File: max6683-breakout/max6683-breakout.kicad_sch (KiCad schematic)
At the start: 11 parts, among them J1 Conn_01x05, J2 Conn_01x05, U1 MAX6683

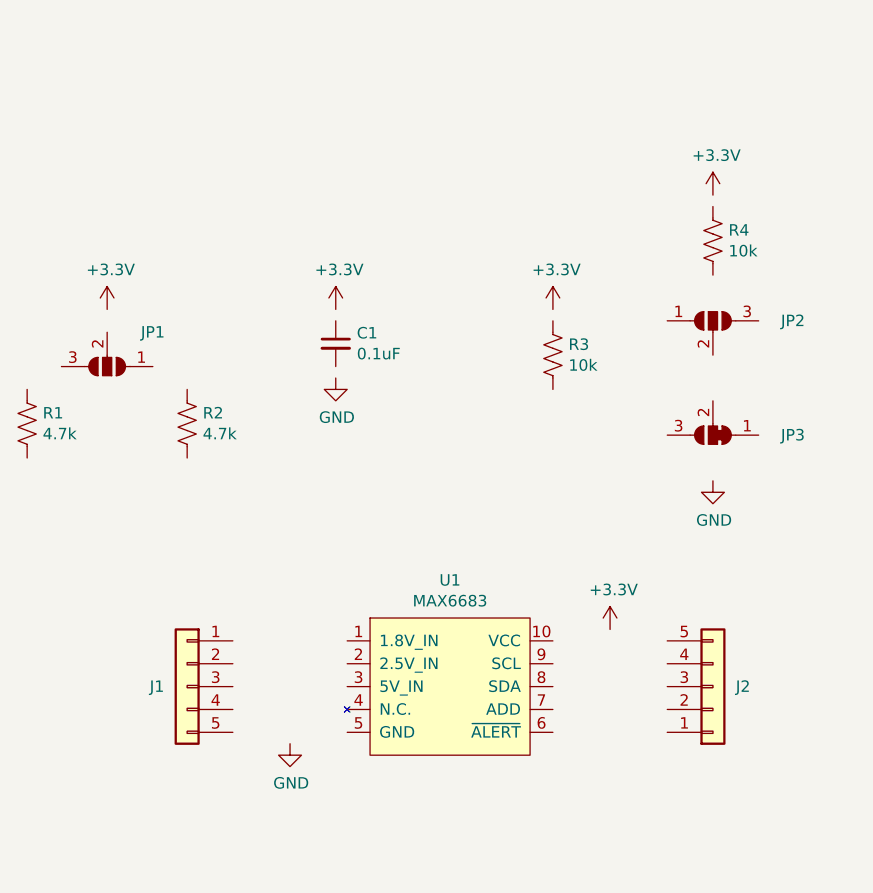
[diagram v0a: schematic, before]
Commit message: Connect schematic nets
Supports #44.
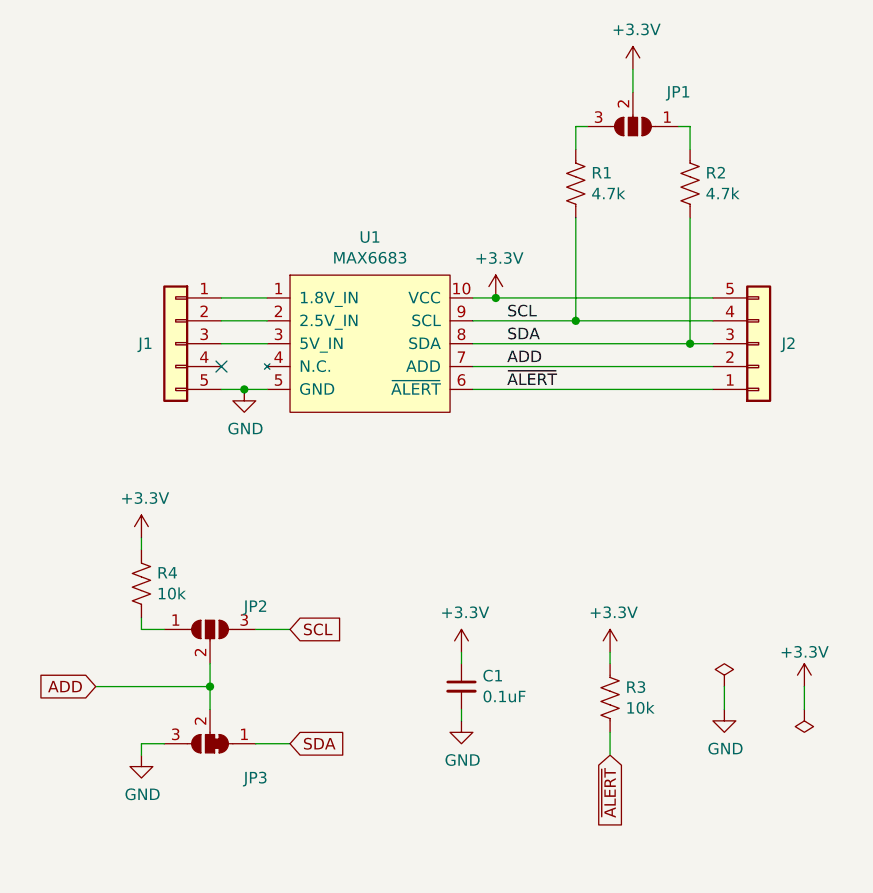
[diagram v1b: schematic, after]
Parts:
- JP1, JP2: value (none) -> SolderJumper_3_Open; footprint (none) -> Jumper:SolderJumper-3_P1.3mm_Open_RoundedPad1.0x1.5mm
- JP3: value (none) -> SolderJumper_3_Bridged12; footprint (none) -> Jumper:SolderJumper-3_P1.3mm_Bridged12_RoundedPad1.0x1.5mm
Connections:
- net +3V3: now also C1.1, J2.5 (Pin_5), JP1.2 (C), R3.1, R4.1, U1.10 (VCC)
- net GND: now also C1.2, J1.5 (Pin_5), JP3.3 (B), U1.5 (GND)
- net at U1.1 (1.8V_IN): now also J1.1 (Pin_1)
- net at U1.2 (2.5V_IN): now also J1.2 (Pin_2)
- net at U1.3 (5V_IN): now also J1.3 (Pin_3)
- net ~{ALERT}: now reaches U1.6 (~{ALERT})
- net ~{ALERT}: now also J2.1 (Pin_1), R3.2
- net ADD: now reaches U1.7 (ADD)
- net ADD: now also J2.2 (Pin_2), JP2.2 (C), JP3.2 (C)
- net SDA: now reaches U1.8 (SDA)
- net SDA: now also J2.3 (Pin_3), JP3.1 (A), R2.2
- net SCL: now reaches U1.9 (SCL)
- net SCL: now also J2.4 (Pin_4), JP2.3 (B), R1.2
- net at R1.1: now also JP1.3 (B)
- net at R2.1: now also JP1.1 (A)
- net at R4.2: now also JP2.1 (A)
- no-connect marks 0 -> 1
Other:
- moved on the sheet: C1, J1, J2, JP1, JP2, JP3, R1, R2, R3, R4, U1

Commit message: Update I2C pullup resistor value
Supports #44.
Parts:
- R1, R2: value 4.7k -> (none); footprint Resistor_SMD:R_0603_1608Metric -> (none); Part Number ERJ-3EKF4701V -> ERJ-3EKF2201V
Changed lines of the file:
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@@
       (effects (font (size 1.27 1.27)) (justify left))
     )
-    (property "Value" "4.7k" (id 1) (at 160.4772 64.643 0)
-      (effects (font (size 1.27 1.27)) (justify left))
-    )
-    (property "Footprint" "Resistor_SMD:R_0603_1608Metric" (id 2) (at 159.766 63.754 90)
+    (property "Value" "" (id 1) (at 160.4772 64.643 0)
+      (effects (font (size 1.27 1.27)) (justify left))
+    )
+    (property "Footprint" "" (id 2) (at 159.766 63.754 90)
       (effects (font (size 1.27 1.27)) hide)
     )
@@
       (effects (font (size 1.27 1.27)) hide)
     )
-    (property "Part Number" "ERJ-3EKF4701V" (id 4) (at 158.75 63.5 0)
+    (property "Part Number" "ERJ-3EKF2201V" (id 4) (at 158.75 63.5 0)
       (effects (font (size 1.27 1.27)) hide)
     )
@@
       (effects (font (size 1.27 1.27)) (justify left))
     )
-    (property "Value" "4.7k" (id 1) (at 173.1772 64.643 0)
-      (effects (font (size 1.27 1.27)) (justify left))
-    )
-    (property "Footprint" "Resistor_SMD:R_0603_1608Metric" (id 2) (at 172.466 63.754 90)
+    (property "Value" "" (id 1) (at 173.1772 64.643 0)
+      (effects (font (size 1.27 1.27)) (justify left))
+    )
+    (property "Footprint" "" (id 2) (at 172.466 63.754 90)
       (effects (font (size 1.27 1.27)) hide)
     )
@@
       (effects (font (size 1.27 1.27)) hide)
     )
-    (property "Part Number" "ERJ-3EKF4701V" (id 4) (at 171.45 63.5 0)
+    (property "Part Number" "ERJ-3EKF2201V" (id 4) (at 171.45 63.5 0)
       (effects (font (size 1.27 1.27)) hide)
     )
@@
       (effects (font (size 1.27 1.27)) hide)
     )
-    (property "Value" "" (id 1) (at 175.26 115.57 0))
+    (property "Value" "PWR_FLAG" (id 1) (at 175.26 115.57 0))
     (property "Footprint" "" (id 2) (at 175.26 119.38 0)
       (effects (font (size 1.27 1.27)) hide)
@@
       (effects (font (size 1.27 1.27)) hide)
     )
-    (property "Value" "" (id 1) (at 184.15 125.73 0))
+    (property "Value" "PWR_FLAG" (id 1) (at 184.15 125.73 0))
     (property "Footprint" "" (id 2) (at 184.15 121.92 0)
       (effects (font (size 1.27 1.27)) hide)
@@
     )
     (path "/00000000-0000-0000-0000-00006201c9d1"
-      (reference "R1") (unit 1) (value "4.7k") (footprint "Resistor_SMD:R_0603_1608Metric")
+      (reference "R1") (unit 1) (value "2.2k") (footprint "Resistor_SMD:R_0603_1608Metric")
     )
     (path "/00000000-0000-0000-0000-0000620b838e"
-      (reference "R2") (unit 1) (value "4.7k") (footprint "Resistor_SMD:R_0603_1608Metric")
+      (reference "R2") (unit 1) (value "2.2k") (footprint "Resistor_SMD:R_0603_1608Metric")
     )
     (path "/00000000-0000-0000-0000-0000620b8c4a"

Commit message: Remove solder jumpers and power flags from BOM
Supports #44.
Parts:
- JP1, JP2: value SolderJumper_3_Open -> (none); footprint Jumper:SolderJumper-3_P1.3mm_Open_RoundedPad1.0x1.5mm -> (none); now left out of the parts list
- JP3: value SolderJumper_3_Bridged12 -> (none); footprint Jumper:SolderJumper-3_P1.3mm_Bridged12_RoundedPad1.0x1.5mm -> (none); now left out of the parts list
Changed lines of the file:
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@@
   )
   (symbol (lib_id "power:+3.3V") (at 165.1 50.8 0) (unit 1)
-    (in_bom yes) (on_board yes)
+    (in_bom no) (on_board yes)
     (property "Reference" "#PWR0101" (id 0) (at 165.1 54.61 0)
       (effects (font (size 1.27 1.27)) hide)
     )
-    (property "Value" "+3.3V" (id 1) (at 165.481 46.4058 0))
+    (property "Value" "" (id 1) (at 165.481 46.4058 0))
     (property "Footprint" "" (id 2) (at 165.1 50.8 0)
       (effects (font (size 1.27 1.27)) hide)
@@
   )
   (symbol (lib_id "power:+3.3V") (at 149.86 76.2 0) (unit 1)
-    (in_bom yes) (on_board yes)
+    (in_bom no) (on_board yes)
     (property "Reference" "#PWR0102" (id 0) (at 149.86 80.01 0)
       (effects (font (size 1.27 1.27)) hide)
     )
-    (property "Value" "+3.3V" (id 1) (at 150.241 71.8058 0))
+    (property "Value" "" (id 1) (at 150.241 71.8058 0))
     (property "Footprint" "" (id 2) (at 149.86 76.2 0)
       (effects (font (size 1.27 1.27)) hide)
@@
   )
   (symbol (lib_id "power:GND") (at 121.92 86.36 0) (unit 1)
-    (in_bom yes) (on_board yes)
+    (in_bom no) (on_board yes)
     (property "Reference" "#PWR0103" (id 0) (at 121.92 92.71 0)
       (effects (font (size 1.27 1.27)) hide)
     )
-    (property "Value" "GND" (id 1) (at 122.047 90.7542 0))
+    (property "Value" "" (id 1) (at 122.047 90.7542 0))
     (property "Footprint" "" (id 2) (at 121.92 86.36 0)
       (effects (font (size 1.27 1.27)) hide)
@@
   )
   (symbol (lib_id "power:GND") (at 110.49 127 0) (unit 1)
-    (in_bom yes) (on_board yes)
+    (in_bom no) (on_board yes)
     (property "Reference" "#PWR0104" (id 0) (at 110.49 133.35 0)
       (effects (font (size 1.27 1.27)) hide)
     )
-    (property "Value" "GND" (id 1) (at 110.617 131.3942 0))
+    (property "Value" "" (id 1) (at 110.617 131.3942 0))
     (property "Footprint" "" (id 2) (at 110.49 127 0)
       (effects (font (size 1.27 1.27)) hide)
@@
   )
   (symbol (lib_id "power:+3.3V") (at 146.05 115.57 0) (unit 1)
-    (in_bom yes) (on_board yes)
+    (in_bom no) (on_board yes)
     (property "Reference" "#PWR0105" (id 0) (at 146.05 119.38 0)
       (effects (font (size 1.27 1.27)) hide)
     )
-    (property "Value" "+3.3V" (id 1) (at 146.431 111.1758 0))
+    (property "Value" "" (id 1) (at 146.431 111.1758 0))
     (property "Footprint" "" (id 2) (at 146.05 115.57 0)
       (effects (font (size 1.27 1.27)) hide)
@@
   )
   (symbol (lib_id "power:GND") (at 146.05 123.19 0) (unit 1)
-    (in_bom yes) (on_board yes)
+    (in_bom no) (on_board yes)
     (property "Reference" "#PWR0106" (id 0) (at 146.05 129.54 0)
       (effects (font (size 1.27 1.27)) hide)
     )
-    (property "Value" "GND" (id 1) (at 146.177 127.5842 0))
+    (property "Value" "" (id 1) (at 146.177 127.5842 0))
     (property "Footprint" "" (id 2) (at 146.05 123.19 0)
       (effects (font (size 1.27 1.27)) hide)
@@
   )
   (symbol (lib_id "power:+3.3V") (at 162.56 115.57 0) (unit 1)
-    (in_bom yes) (on_board yes)
+    (in_bom no) (on_board yes)
     (property "Reference" "#PWR0107" (id 0) (at 162.56 119.38 0)
       (effects (font (size 1.27 1.27)) hide)
     )
-    (property "Value" "+3.3V" (id 1) (at 162.941 111.1758 0))
+    (property "Value" "" (id 1) (at 162.941 111.1758 0))
     (property "Footprint" "" (id 2) (at 162.56 115.57 0)
       (effects (font (size 1.27 1.27)) hide)
@@
   )
   (symbol (lib_id "power:+3.3V") (at 110.49 102.87 0) (unit 1)
-    (in_bom yes) (on_board yes)
+    (in_bom no) (on_board yes)
     (property "Reference" "#PWR0108" (id 0) (at 110.49 106.68 0)
       (effects (font (size 1.27 1.27)) hide)
     )
-    (property "Value" "+3.3V" (id 1) (at 110.871 98.4758 0))
+    (property "Value" "" (id 1) (at 110.871 98.4758 0))
     (property "Footprint" "" (id 2) (at 110.49 102.87 0)
       (effects (font (size 1.27 1.27)) hide)
@@
   )
   (symbol (lib_id "Jumper:SolderJumper_3_Bridged12") (at 118.11 125.73 180) (unit 1)
-    (in_bom yes) (on_board yes)
+    (in_bom no) (on_board yes)
     (property "Reference" "JP3" (id 0) (at 123.19 129.54 0))
-    (property "Value" "SolderJumper_3_Bridged12" (id 1) (at 118.11 129.54 0)
-      (effects (font (size 1.27 1.27)) hide)
-    )
-    (property "Footprint" "Jumper:SolderJumper-3_P1.3mm_Bridged12_RoundedPad1.0x1.5mm" (id 2) (at 118.11 125.73 0)
+    (property "Value" "" (id 1) (at 118.11 129.54 0)
+      (effects (font (size 1.27 1.27)) hide)
+    )
+    (property "Footprint" "" (id 2) (at 118.11 125.73 0)
       (effects (font (size 1.27 1.27)) hide)
     )
@@
   )
   (symbol (lib_id "power:GND") (at 175.26 121.92 0) (unit 1)
-    (in_bom yes) (on_board yes)
+    (in_bom no) (on_board yes)
     (property "Reference" "#PWR01" (id 0) (at 175.26 128.27 0)
       (effects (font (size 1.27 1.27)) hide)
     )
-    (property "Value" "GND" (id 1) (at 175.387 126.3142 0))
+    (property "Value" "" (id 1) (at 175.387 126.3142 0))
     (property "Footprint" "" (id 2) (at 175.26 121.92 0)
       (effects (font (size 1.27 1.27)) hide)
@@
   )
   (symbol (lib_id "power:+3.3V") (at 184.15 119.38 0) (unit 1)
-    (in_bom yes) (on_board yes)
+    (in_bom no) (on_board yes)
     (property "Reference" "#PWR02" (id 0) (at 184.15 123.19 0)
       (effects (font (size 1.27 1.27)) hide)
     )
-    (property "Value" "+3.3V" (id 1) (at 184.15 115.57 0))
+    (property "Value" "" (id 1) (at 184.15 115.57 0))
     (property "Footprint" "" (id 2) (at 184.15 119.38 0)
       (effects (font (size 1.27 1.27)) hide)
@@
   )
   (symbol (lib_id "power:PWR_FLAG") (at 175.26 119.38 0) (unit 1)
-    (in_bom yes) (on_board yes)
+    (in_bom no) (on_board yes)
     (property "Reference" "#FLG01" (id 0) (at 175.26 117.475 0)
       (effects (font (size 1.27 1.27)) hide)
     )
-    (property "Value" "PWR_FLAG" (id 1) (at 175.26 115.57 0))
+    (property "Value" "" (id 1) (at 175.26 115.57 0))
     (property "Footprint" "" (id 2) (at 175.26 119.38 0)
       (effects (font (size 1.27 1.27)) hide)
@@
   )
   (symbol (lib_id "power:PWR_FLAG") (at 184.15 121.92 180) (unit 1)
-    (in_bom yes) (on_board yes)
+    (in_bom no) (on_board yes)
     (property "Reference" "#FLG02" (id 0) (at 184.15 123.825 0)
       (effects (font (size 1.27 1.27)) hide)
     )
-    (property "Value" "PWR_FLAG" (id 1) (at 184.15 125.73 0))
+    (property "Value" "" (id 1) (at 184.15 125.73 0))
     (property "Footprint" "" (id 2) (at 184.15 121.92 0)
       (effects (font (size 1.27 1.27)) hide)
@@
   )
   (symbol (lib_id "Jumper:SolderJumper_3_Open") (at 118.11 113.03 0) (unit 1)
-    (in_bom yes) (on_board yes)
+    (in_bom no) (on_board yes)
     (property "Reference" "JP2" (id 0) (at 123.19 110.49 0))
-    (property "Value" "SolderJumper_3_Open" (id 1) (at 118.11 109.22 0)
-      (effects (font (size 1.27 1.27)) hide)
-    )
-    (property "Footprint" "Jumper:SolderJumper-3_P1.3mm_Open_RoundedPad1.0x1.5mm" (id 2) (at 118.11 113.03 0)
+    (property "Value" "" (id 1) (at 118.11 109.22 0)
+      (effects (font (size 1.27 1.27)) hide)
+    )
+    (property "Footprint" "" (id 2) (at 118.11 113.03 0)
       (effects (font (size 1.27 1.27)) hide)
     )
@@
   )
   (symbol (lib_id "Jumper:SolderJumper_3_Open") (at 165.1 57.15 180) (unit 1)
-    (in_bom yes) (on_board yes)
+    (in_bom no) (on_board yes)
     (property "Reference" "JP1" (id 0) (at 170.18 53.34 0))
-    (property "Value" "SolderJumper_3_Open" (id 1) (at 165.1 63.5 0)
-      (effects (font (size 1.27 1.27)) hide)
-    )
-    (property "Footprint" "Jumper:SolderJumper-3_P1.3mm_Open_RoundedPad1.0x1.5mm" (id 2) (at 165.1 57.15 0)
-      (effects (font (size 1.27 1.27)) hide)
-    )
+    (property "Value" "" (id 1) (at 165.1 63.5 0)
+      (effects (font (size 1.27 1.27)) hide)
+    )
+    (property "Footprint" "" (id 2) (at 165.1 57.15 0)
+      (effects (font (size 1.27 1.27)) hide)
+    )
